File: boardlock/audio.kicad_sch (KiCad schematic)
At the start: 20 parts, among them J3 5033981892, J4 Conn_01x02, J5 Conn_01x02, Q2 MMBT4401, Q4 BSS84PWH6327XTSA1, U7 MAX98357AETE+T

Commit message: footprints finished for now
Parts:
- R7, R8, R?: footprint (none) -> Resistor_SMD:R_0805_2012Metric_Pad1.20x1.40mm_HandSolder
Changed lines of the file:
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@@
       (effects (font (size 1.27 1.27)) (justify left))
     )
-    (property "Footprint" "" (at 205.486 105.664 90)
+    (property "Footprint" "Resistor_SMD:R_0805_2012Metric_Pad1.20x1.40mm_HandSolder" (at 205.486 105.664 90)
       (effects (font (size 1.27 1.27)) hide)
     )
@@
       (effects (font (size 1.27 1.27)) (justify left))
     )
-    (property "Footprint" "" (at 192.786 124.714 90)
+    (property "Footprint" "Resistor_SMD:R_0805_2012Metric_Pad1.20x1.40mm_HandSolder" (at 192.786 124.714 90)
       (effects (font (size 1.27 1.27)) hide)
     )
@@
       (effects (font (size 1.27 1.27)))
     )
-    (property "Footprint" "" (at 184.404 118.364 90)
-      (effects (font (size 1.27 1.27)) hide)
-    )
+    (property "Footprint" "Resistor_SMD:R_0805_2012Metric_Pad1.20x1.40mm_HandSolder" (at 184.404 118.364 90)
+      (effects (font (size 1.27 1.27)) hide)
+    )

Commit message: more pcb stuff
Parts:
- renumbered C30 to C23, C13 to C24, C14 to C25, C31 to C26, C32 to C27, C33 to C28, J4 to J3, J5 to J4, J3 to J5, R56 to R35, R57 to R36, R58 to R37, U7 to U8

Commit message: buck-boost WIP
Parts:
- J3: footprint Connector_JST:JST_XA_B02B-XASK-1-A_1x02_P2.50mm_Vertical -> Connector_JST:JST_XA_B02B-XASK-1_1x02_P2.50mm_Vertical
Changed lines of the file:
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@@
       (effects (font (size 1.27 1.27)) (justify left))
     )
-    (property "Footprint" "Connector_JST:JST_XA_B02B-XASK-1-A_1x02_P2.50mm_Vertical" (at 203.2 55.88 0)
+    (property "Footprint" "Connector_JST:JST_XA_B02B-XASK-1_1x02_P2.50mm_Vertical" (at 203.2 55.88 0)
       (effects (font (size 1.27 1.27)) hide)
     )

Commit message: boost conveter complete
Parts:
- removed Q2: MMBT4401, Package_TO_SOT_SMD:SOT-23-3, symbol Device:Q_NPN_BCE
- removed R8, R?: R_US, Resistor_SMD:R_0805_2012Metric_Pad1.20x1.40mm_HandSolder, symbol Device:R_US
- added Q7: DTC124X, Package_TO_SOT_SMD:SOT-23_Handsoldering, symbol Transistor_BJT:DTC124X
- J4: footprint Connector_JST:JST_XA_B02B-XASK-1-A_1x02_P2.50mm_Vertical -> Connector_JST:JST_XA_B02B-XASK-1_1x02_P2.50mm_Vertical
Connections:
- net GND: now also Q7.2 (E)
- net M_BUZZER_EN: now also Q7.1 (B)
- net at Q4.1 (G), R7.2: now also Q7.3 (C)
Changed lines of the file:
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@@
   (junction (at 147.32 71.12) (diameter 0) (color 0 0 0 0)
   )
-  (junction (at 204.47 129.54) (diameter 0) (color 0 0 0 0)
-  )
   (junction (at 73.66 39.37) (diameter 0) (color 0 0 0 0)
   )
@@
   )
   (junction (at 135.89 74.93) (diameter 0) (color 0 0 0 0)
-  )
-  (junction (at 191.77 119.38) (diameter 0) (color 0 0 0 0)
   )
   (junction (at 160.02 53.34) (diameter 0) (color 0 0 0 0)
@@
     (stroke (width 0) (type default))
   )
-  (wire (pts (xy 191.77 129.54) (xy 204.47 129.54))
-    (stroke (width 0) (type default))
-  )
   (wire (pts (xy 120.65 153.67) (xy 120.65 154.94))
     (stroke (width 0) (type default))
@@
     (stroke (width 0) (type default))
   )
-  (wire (pts (xy 191.77 119.38) (xy 191.77 120.65))
-    (stroke (width 0) (type default))
-  )
   (wire (pts (xy 74.93 133.35) (xy 76.2 133.35))
     (stroke (width 0) (type default))
@@
     (stroke (width 0) (type default))
   )
-  (wire (pts (xy 187.96 119.38) (xy 191.77 119.38))
-    (stroke (width 0) (type default))
-  )
   (wire (pts (xy 62.23 36.83) (xy 62.23 39.37))
     (stroke (width 0) (type default))
@@
     (stroke (width 0) (type default))
   )
-  (wire (pts (xy 191.77 119.38) (xy 196.85 119.38))
-    (stroke (width 0) (type default))
-  )
   (wire (pts (xy 135.89 72.39) (xy 135.89 74.93))
     (stroke (width 0) (type default))
@@
     (stroke (width 0) (type default))
   )
-  (wire (pts (xy 175.26 119.38) (xy 180.34 119.38))
+  (wire (pts (xy 190.5 119.38) (xy 195.58 119.38))
     (stroke (width 0) (type default))
   )
@@
     (stroke (width 0) (type default))
   )
-  (wire (pts (xy 204.47 129.54) (xy 204.47 130.81))
-    (stroke (width 0) (type default))
-  )
   (wire (pts (xy 132.08 77.47) (xy 135.89 77.47))
     (stroke (width 0) (type default))
@@
     (stroke (width 0) (type default))
   )
-  (wire (pts (xy 191.77 128.27) (xy 191.77 129.54))
-    (stroke (width 0) (type default))
-  )
   (wire (pts (xy 73.66 49.53) (xy 85.09 49.53))
     (stroke (width 0) (type default))
@@
     (stroke (width 0) (type default))
   )
-  (wire (pts (xy 204.47 127) (xy 204.47 129.54))
+  (wire (pts (xy 204.47 127) (xy 204.47 130.81))
     (stroke (width 0) (type default))
   )
@@
     )
   )
-  (global_label "M_BUZZER_EN" (shape input) (at 175.26 119.38 180) (fields_autoplaced)
+  (global_label "M_BUZZER_EN" (shape input) (at 190.5 119.38 180) (fields_autoplaced)
     (effects (font (size 1.27 1.27)) (justify right))
-    (property "Intersheetrefs" "${INTERSHEET_REFS}" (at 158.9702 119.38 0)
+    (property "Intersheetrefs" "${INTERSHEET_REFS}" (at 174.2102 119.38 0)
       (effects (font (size 1.27 1.27)) (justify right) hide)
     )
@@
     )
   )
+  (symbol (lib_id "Transistor_BJT:DTC124X") (at 201.93 119.38 0) (unit 1)
+    (in_bom yes) (on_board yes) (dnp no) (fields_autoplaced)
+    (property "Reference" "Q7" (at 207.01 118.745 0)
+      (effects (font (size 1.27 1.27)) (justify left))
+    )
+    (property "Value" "DTC124X" (at 207.01 121.285 0)
+      (effects (font (size 1.27 1.27)) (justify left))
+    )
+    (property "Footprint" "Package_TO_SOT_SMD:SOT-23_Handsoldering" (at 201.93 119.38 0)
+      (effects (font (size 1.27 1.27)) (justify left) hide)
+    )
+    (property "Datasheet" "" (at 201.93 119.38 0)
+      (effects (font (size 1.27 1.27)) (justify left) hide)
+    )
+    (pin "1")
+    (pin "2")
+    (pin "3")
+    (instances
+      (project "boardlock"
+        (path "/e1fc29ce-837e-4062-84d8-c7e423f9eab9/c1e95beb-a482-4f8e-b13b-3641abb17f9b"
+          (reference "Q7") (unit 1)
+        )
+        (path "/e1fc29ce-837e-4062-84d8-c7e423f9eab9/1eb676fb-9e7a-4e01-ba1e-2eff94d7b66e"
+          (reference "Q4") (unit 1)
+        )
+      )
+    )
+  )
   (symbol (lib_id "Connector_Generic:Conn_01x02") (at 246.38 124.46 0) (unit 1)
     (in_bom yes) (on_board yes) (dnp no) (fields_autoplaced)
@@
       (effects (font (size 1.27 1.27)) (justify left))
     )
-    (property "Footprint" "Connector_JST:JST_XA_B02B-XASK-1-A_1x02_P2.50mm_Vertical" (at 246.38 124.46 0)
+    (property "Footprint" "Connector_JST:JST_XA_B02B-XASK-1_1x02_P2.50mm_Vertical" (at 246.38 124.46 0)
       (effects (font (size 1.27 1.27)) hide)
     )
@@
         (path "/e1fc29ce-837e-4062-84d8-c7e423f9eab9/1eb676fb-9e7a-4e01-ba1e-2eff94d7b66e"
           (reference "R37") (unit 1)
-        )
-      )
-    )
-  )
-  (symbol (lib_id "Device:R_US") (at 191.77 124.46 0) (unit 1)
-    (in_bom yes) (on_board yes) (dnp no) (fields_autoplaced)
-    (property "Reference" "R?" (at 194.31 123.19 0)
-      (effects (font (size 1.27 1.27)) (justify left))
-    )
-    (property "Value" "R_US" (at 194.31 125.73 0)
-      (effects (font (size 1.27 1.27)) (justify left))
-    )
-    (property "Footprint" "Resistor_SMD:R_0805_2012Metric_Pad1.20x1.40mm_HandSolder" (at 192.786 124.714 90)
-      (effects (font (size 1.27 1.27)) hide)
-    )
-    (property "Datasheet" "~" (at 191.77 124.46 0)
-      (effects (font (size 1.27 1.27)) hide)
-    )
-    (pin "1")
-    (pin "2")
-    (instances
-      (project "boardlock"
-        (path "/e1fc29ce-837e-4062-84d8-c7e423f9eab9/a4a6f965-a4d9-4da6-b64e-79eda0daabe5"
-          (reference "R?") (unit 1)
-        )
-        (path "/e1fc29ce-837e-4062-84d8-c7e423f9eab9/1eb676fb-9e7a-4e01-ba1e-2eff94d7b66e"
-          (reference "R40") (unit 1)
         )
       )
@@
         )
       )
-    )
-  )
-  (symbol (lib_id "Device:R_US") (at 184.15 119.38 90) (unit 1)
-    (in_bom yes) (on_board yes) (dnp no) (fields_autoplaced)
-    (property "Reference" "R8" (at 184.15 114.3467 90)
-      (effects (font (size 1.27 1.27)))
-    )
-    (property "Value" "R_US" (at 184.15 116.7709 90)
-      (effects (font (size 1.27 1.27)))
-    )
-    (property "Footprint" "Resistor_SMD:R_0805_2012Metric_Pad1.20x1.40mm_HandSolder" (at 184.404 118.364 90)
-      (effects (font (size 1.27 1.27)) hide)
-    )
-    (property "Datasheet" "~" (at 184.15 119.38 0)
-      (effects (font (size 1.27 1.27)) hide)
-    )
-    (pin "1")
-    (pin "2")
-    (instances
-      (project "boardlock"
-        (path "/48f24f42-fd64-4860-9f12-ca34cf195758/17b4aebf-aea4-4bb2-a07c-86de8cf47820"
-          (reference "R8") (unit 1)
-        )
-      )
-      (project "boardlock"
-        (path "/e1fc29ce-837e-4062-84d8-c7e423f9eab9/a4a6f965-a4d9-4da6-b64e-79eda0daabe5"
-          (reference "R16") (unit 1)
-        )
-        (path "/e1fc29ce-837e-4062-84d8-c7e423f9eab9/1eb676fb-9e7a-4e01-ba1e-2eff94d7b66e"
-          (reference "R39") (unit 1)
-        )
-      )
-    )
-  )
-  (symbol (lib_id "Device:Q_NPN_BCE") (at 201.93 119.38 0) (unit 1)
-    (in_bom yes) (on_board yes) (dnp no) (fields_autoplaced)
-    (property "Reference" "Q2" (at 207.01 118.11 0)
-      (effects (font (size 1.27 1.27)) (justify left))
-    )
-    (property "Value" "MMBT4401" (at 207.01 120.65 0)
-      (effects (font (size 1.27 1.27)) (justify left))
-    )
-    (property "Footprint" "Package_TO_SOT_SMD:SOT-23-3" (at 207.01 116.84 0)
-      (effects (font (size 1.27 1.27)) hide)
-    )
-    (property "Datasheet" "~" (at 201.93 119.38 0)
-      (effects (font (size 1.27 1.27)) hide)
-    )
-    (pin "1")
-    (pin "2")
-    (pin "3")
-    (instances
-      (project "boardlock"
-        (path "/48f24f42-fd64-4860-9f12-ca34cf195758/17b4aebf-aea4-4bb2-a07c-86de8cf47820"
-          (reference "Q2") (unit 1)
-        )
-      )
-      (project "boardlock"
-        (path "/e1fc29ce-837e-4062-84d8-c7e423f9eab9/a4a6f965-a4d9-4da6-b64e-79eda0daabe5"
-          (reference "Q2") (unit 1)
-        )
-        (path "/e1fc29ce-837e-4062-84d8-c7e423f9eab9/1eb676fb-9e7a-4e01-ba1e-2eff94d7b66e"
-          (reference "Q4") (unit 1)
-        )
-      )

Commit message: small edits
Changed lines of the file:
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@@
     (stroke (width 0) (type default))
   )
-  (text "Buzzer Power Circuit" (at 184.15 85.09 0)
+  (text "Buzzer Power Circuit" (at 191.77 87.63 0)
     (effects (font (size 2.5 2.5) (thickness 0.5) bold) (justify left bottom))
   )
@@
     (effects (font (size 1.27 1.27)) (justify left bottom))
   )
-  (text "Double check this circuit with 12V" (at 217.17 93.98 0)
+  (text "Double check this circuit with 12V" (at 246.38 77.47 0)
     (effects (font (size 1.27 1.27)) (justify left bottom))
   )

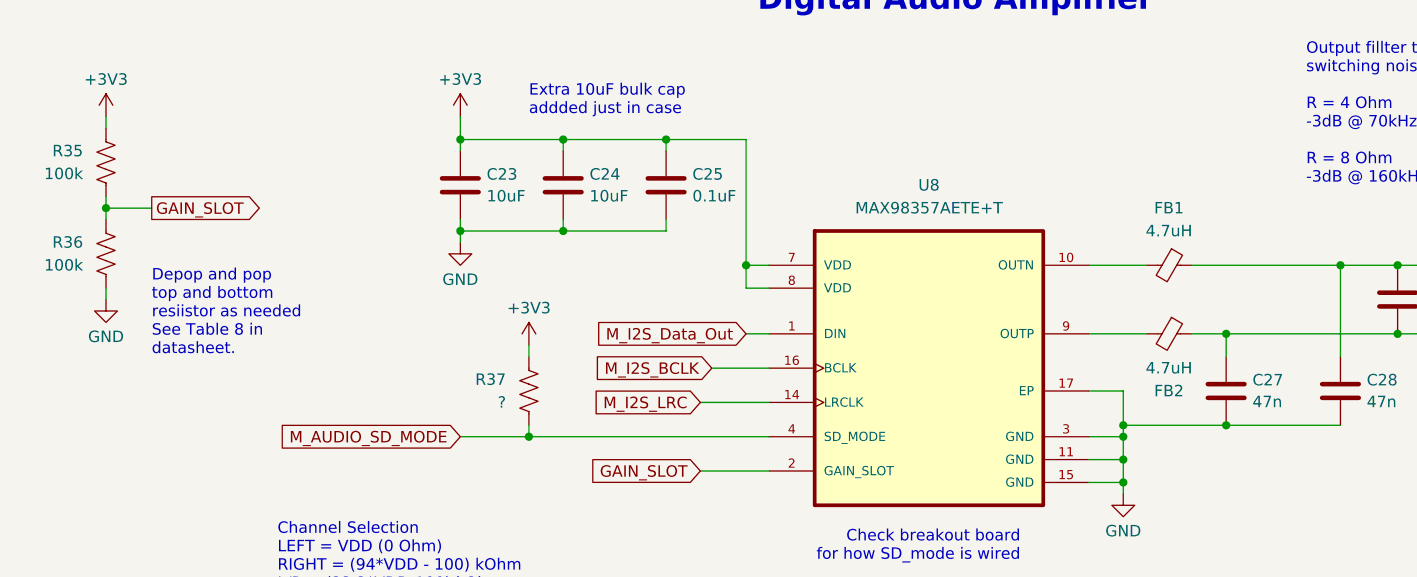
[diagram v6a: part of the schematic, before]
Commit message: Manufacturing and debugging mods in SCH
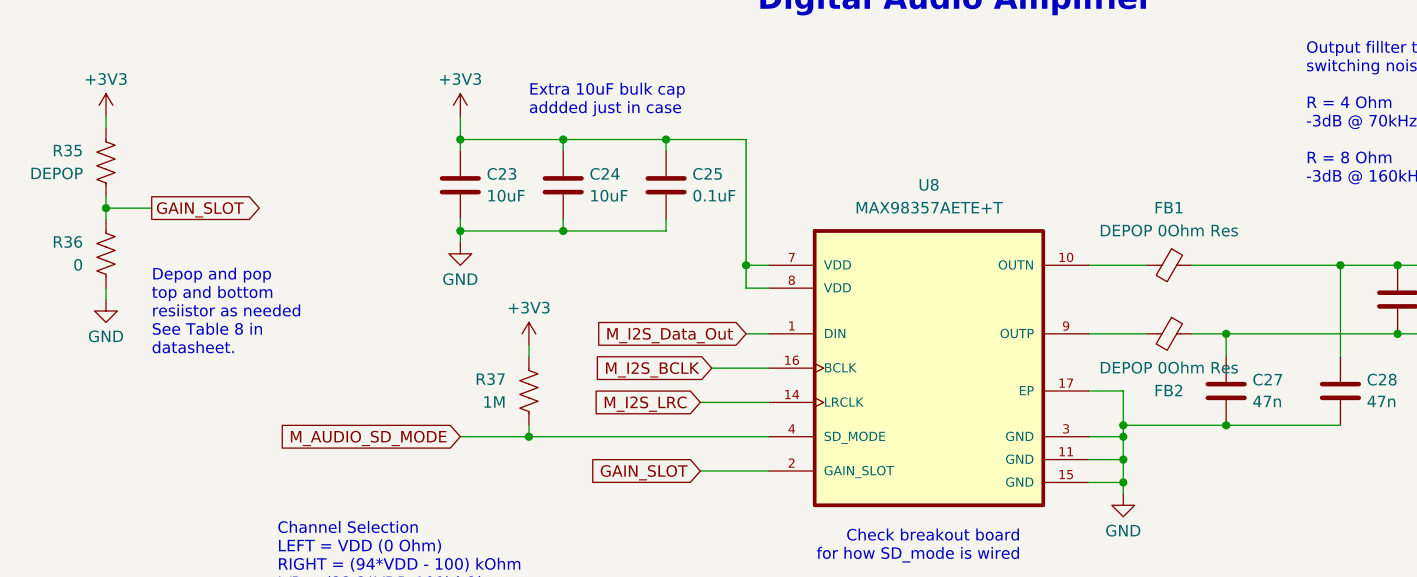
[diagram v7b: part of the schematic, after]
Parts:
- FB1, FB2: value 4.7uH -> DEPOP 0Ohm Res
- R35: value 100k -> DEPOP
- R36: value 100k -> 0
- R37: value ? -> 1M
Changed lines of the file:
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@@
       (effects (font (size 1.27 1.27)))
     )
-    (property "Value" "4.7uH" (at 140.97 49.53 90)
+    (property "Value" "DEPOP 0Ohm Res" (at 140.97 49.53 90)
       (effects (font (size 1.27 1.27)))
     )
@@
       (effects (font (size 1.27 1.27)))
     )
-    (property "Value" "4.7uH" (at 140.97 64.77 90)
+    (property "Value" "DEPOP 0Ohm Res" (at 140.97 64.77 90)
       (effects (font (size 1.27 1.27)))
     )
@@
       (effects (font (size 1.27 1.27)) (justify right))
     )
-    (property "Value" "100k" (at 20.32 53.34 0)
+    (property "Value" "0" (at 20.32 53.34 0)
       (effects (font (size 1.27 1.27)) (justify right))
     )
@@
       (effects (font (size 1.27 1.27)) (justify right))
     )
-    (property "Value" "?" (at 67.31 68.58 0)
+    (property "Value" "1M" (at 67.31 68.58 0)
       (effects (font (size 1.27 1.27)) (justify right))
     )
@@
       (effects (font (size 1.27 1.27)) (justify right))
     )
-    (property "Value" "100k" (at 20.32 43.18 0)
-      (effects (font (size 1.27 1.27)) (justify right))
-    )
+    (property "Value" "DEPOP" (at 20.32 43.18 0)
+      (effects (font (size 1.27 1.27)) (justify right))
+    )
